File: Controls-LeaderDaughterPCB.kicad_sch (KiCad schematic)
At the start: 24 parts, among them U8 LMC555xM

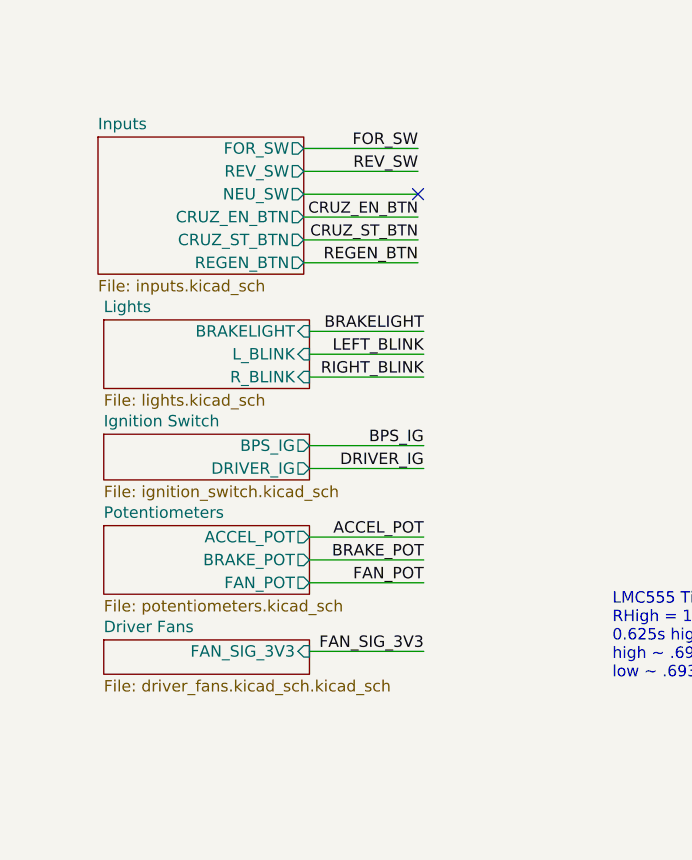
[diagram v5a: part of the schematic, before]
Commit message: Removed neutral section's debouncing circuitry and connections
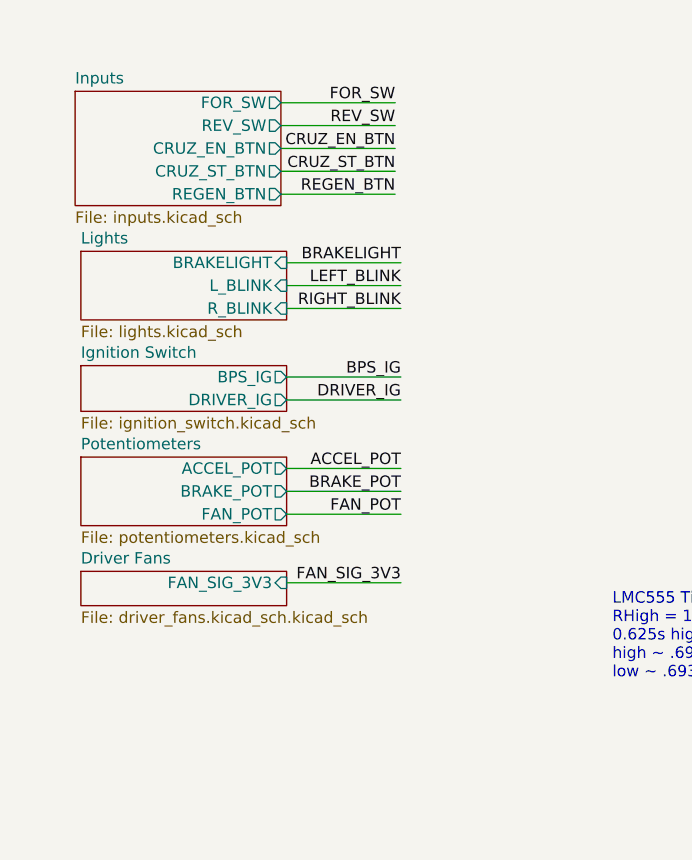
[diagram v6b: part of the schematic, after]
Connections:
- no-connect marks 7 -> 6
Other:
- sheet Inputs ports: added none; removed NEU_SW

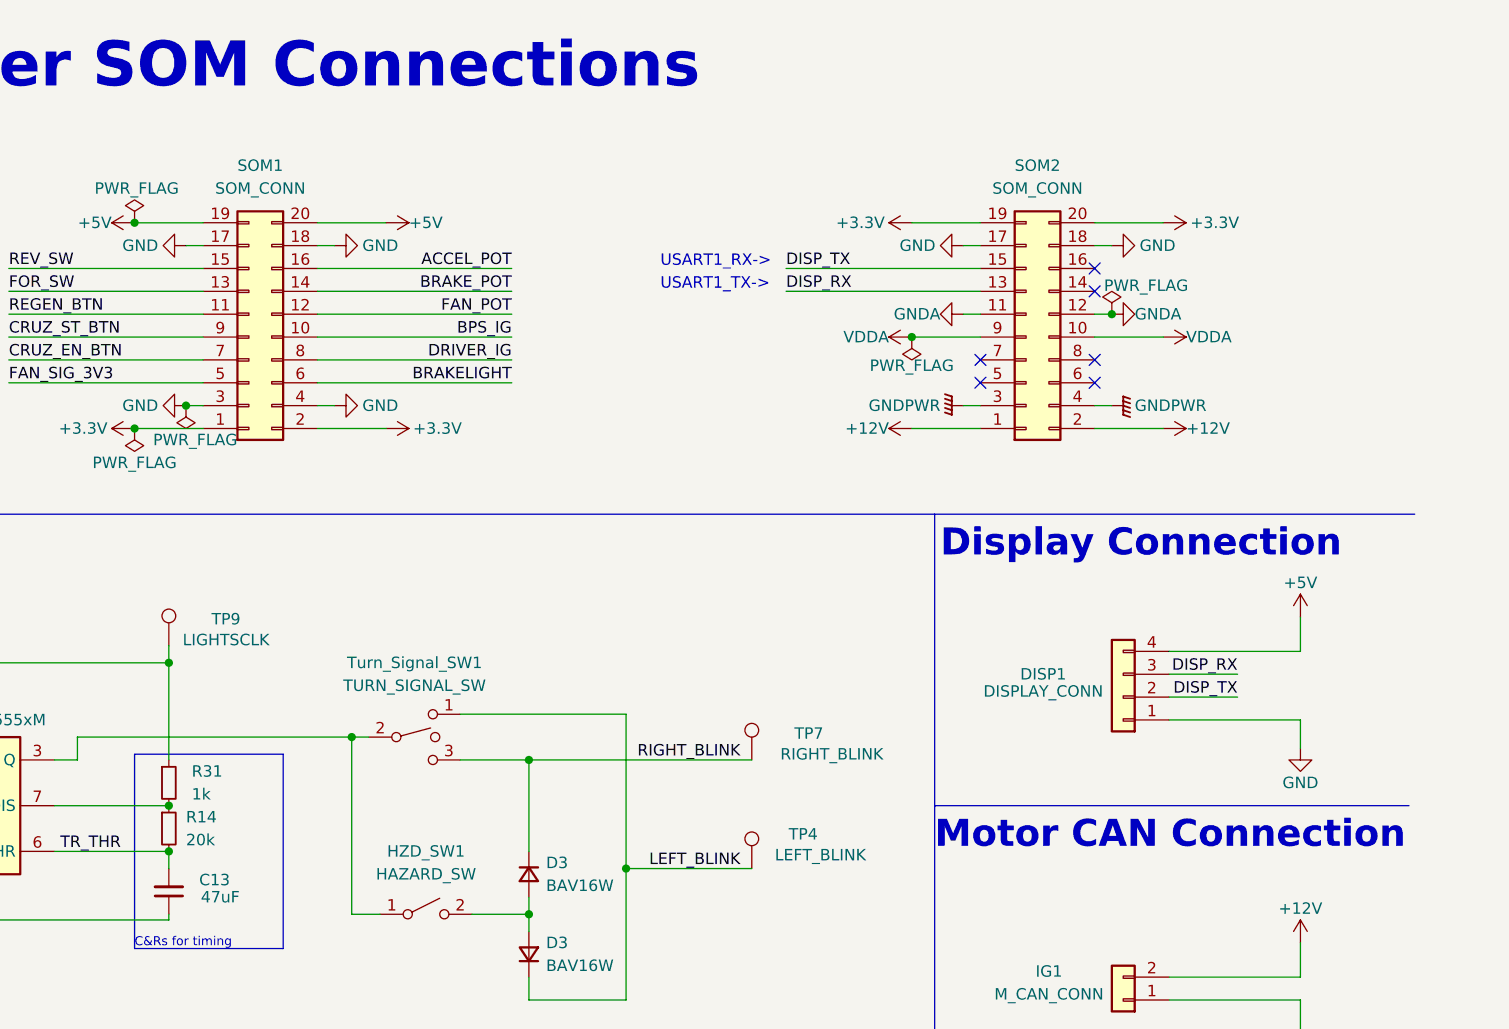
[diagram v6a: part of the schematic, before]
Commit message: Added test points
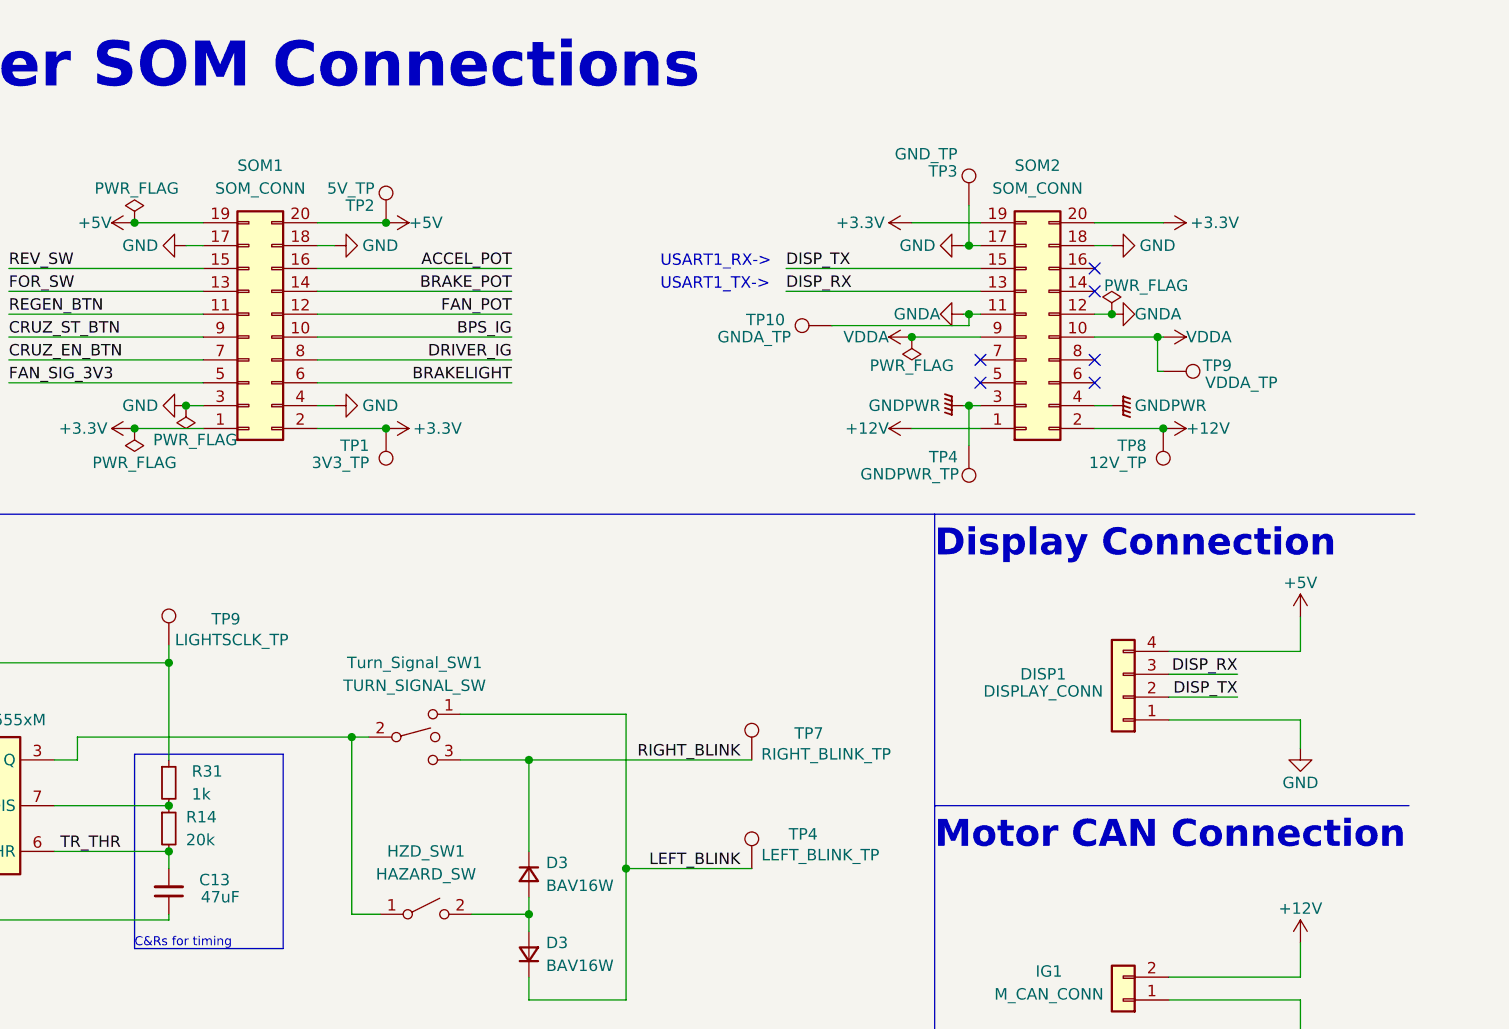
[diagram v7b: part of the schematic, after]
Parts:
- added TP1: 3V3_TP, symbol Connector:TestPoint
- added TP10: GNDA_TP, symbol Connector:TestPoint
- added TP2: 5V_TP, symbol Connector:TestPoint
- added TP3: GND_TP, symbol Connector:TestPoint
- added TP4: GNDPWR_TP, symbol Connector:TestPoint
- added TP8: 12V_TP, symbol Connector:TestPoint
- added TP9: VDDA_TP, symbol Connector:TestPoint
- TP4: value LEFT_BLINK -> LEFT_BLINK_TP
- TP7: value RIGHT_BLINK -> RIGHT_BLINK_TP
- TP9: value LIGHTSCLK -> LIGHTSCLK_TP
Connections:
- net +12V: now also TP8.1
- net +3.3V: now also TP1.1
- net +5V: now also TP2.1
- net GND: now also TP3.1
- net GNDA: now also TP10.1
- net GNDPWR: now also TP4.1
- net VDDA: now also TP9.1

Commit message: Adjusted & added footprints, several minor changes
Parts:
- TP1, TP10, TP2, TP3, TP4, TP8, TP9: footprint (none) -> TestPoint:TestPoint_Pad_1.5x1.5mm
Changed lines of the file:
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@@
       (effects (font (size 1.27 1.27)) (justify right))
     )
-    (property "Footprint" "" (at 241.935 31.75 0)
+    (property "Footprint" "TestPoint:TestPoint_Pad_1.5x1.5mm" (at 241.935 31.75 0)
       (effects (font (size 1.27 1.27)) hide)
     )
@@
       (effects (font (size 1.27 1.27)) (justify right))
     )
-    (property "Footprint" "" (at 231.775 58.42 0)
+    (property "Footprint" "TestPoint:TestPoint_Pad_1.5x1.5mm" (at 231.775 58.42 0)
       (effects (font (size 1.27 1.27)) hide)
     )
@@
       (effects (font (size 1.27 1.27)) (justify right))
     )
-    (property "Footprint" "" (at 177.165 33.655 0)
+    (property "Footprint" "TestPoint:TestPoint_Pad_1.5x1.5mm" (at 177.165 33.655 0)
       (effects (font (size 1.27 1.27)) hide)
     )
@@
       (effects (font (size 1.27 1.27)) (justify right))
     )
-    (property "Footprint" "" (at 253.365 56.515 0)
+    (property "Footprint" "TestPoint:TestPoint_Pad_1.5x1.5mm" (at 253.365 56.515 0)
       (effects (font (size 1.27 1.27)) hide)
     )
@@
       (effects (font (size 1.27 1.27)) (justify right))
     )
-    (property "Footprint" "" (at 221.615 40.005 0)
+    (property "Footprint" "TestPoint:TestPoint_Pad_1.5x1.5mm" (at 221.615 40.005 0)
       (effects (font (size 1.27 1.27)) hide)
     )
@@
       (effects (font (size 1.27 1.27)) (justify right))
     )
-    (property "Footprint" "" (at 167.005 56.515 0)
+    (property "Footprint" "TestPoint:TestPoint_Pad_1.5x1.5mm" (at 167.005 56.515 0)
       (effects (font (size 1.27 1.27)) hide)
     )
@@
       (effects (font (size 1.27 1.27)) (justify right))
     )
-    (property "Footprint" "" (at 258.445 55.245 0)
-      (effects (font (size 1.27 1.27)) hide)
-    )
+    (property "Footprint" "TestPoint:TestPoint_Pad_1.5x1.5mm" (at 258.445 55.245 0)
+      (effects (font (size 1.27 1.27)) hide)
+    )
